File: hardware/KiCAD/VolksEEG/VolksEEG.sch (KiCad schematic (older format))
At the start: 0 parts

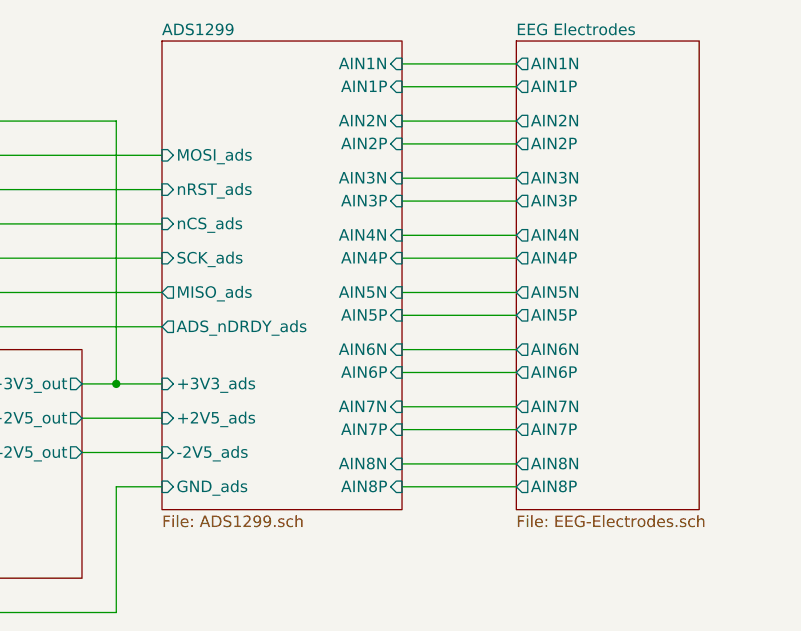
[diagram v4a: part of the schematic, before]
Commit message: Updating analogue inputs to the referential montage and connected a few ADS1299 pins.
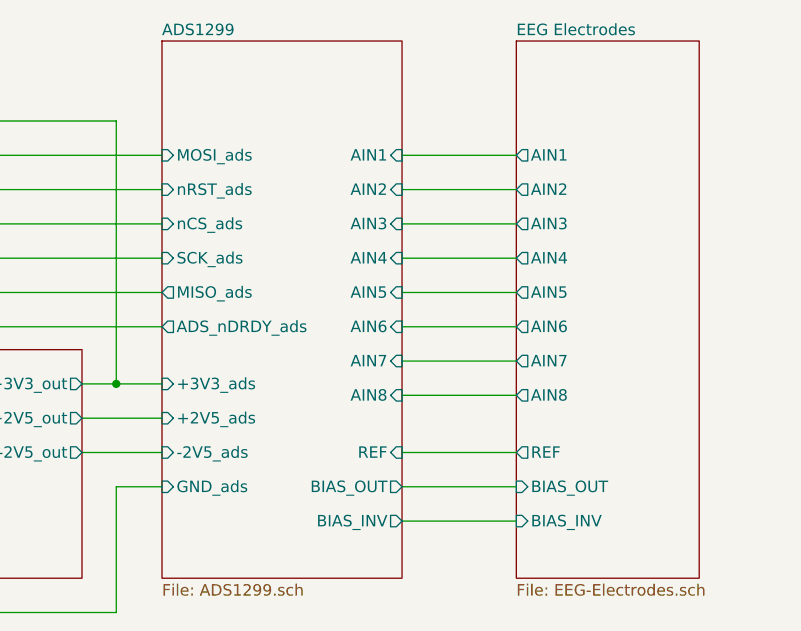
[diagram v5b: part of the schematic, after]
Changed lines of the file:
@@
 $EndDescr
 $Sheet
-S 6600 3000 1050 2050
+S 6600 3000 1050 2350
 U 615BA110
 F0 "ADS1299" 50
@@
 F5 "MISO_ads" O L 6600 4100 50
 F6 "nRST_ads" I L 6600 3650 50
-F7 "AIN5N" I R 7650 4100 50
-F8 "AIN5P" I R 7650 4200 50
-F9 "AIN6N" I R 7650 4350 50
-F10 "AIN6P" I R 7650 4450 50
-F11 "AIN7N" I R 7650 4600 50
-F12 "AIN7P" I R 7650 4700 50
-F13 "AIN8N" I R 7650 4850 50
-F14 "AIN8P" I R 7650 4950 50
-F15 "AIN1N" I R 7650 3100 50
-F16 "AIN1P" I R 7650 3200 50
-F17 "AIN2N" I R 7650 3350 50
-F18 "AIN2P" I R 7650 3450 50
-F19 "AIN3N" I R 7650 3600 50
-F20 "AIN3P" I R 7650 3700 50
-F21 "AIN4N" I R 7650 3850 50
-F22 "AIN4P" I R 7650 3950 50
-F23 "ADS_nDRDY_ads" O L 6600 4250 50
-F24 "+3V3_ads" I L 6600 4500 50
-F25 "+2V5_ads" I L 6600 4650 50
-F26 "-2V5_ads" I L 6600 4800 50
-F27 "GND_ads" I L 6600 4950 50
+F7 "AIN5" I R 7650 4100 50
+F8 "AIN6" I R 7650 4250 50
+F9 "AIN7" I R 7650 4400 50
+F10 "AIN8" I R 7650 4550 50
+F11 "AIN1" I R 7650 3500 50
+F12 "AIN2" I R 7650 3650 50
+F13 "AIN3" I R 7650 3800 50
+F14 "AIN4" I R 7650 3950 50
+F15 "ADS_nDRDY_ads" O L 6600 4250 50
+F16 "+3V3_ads" I L 6600 4500 50
+F17 "+2V5_ads" I L 6600 4650 50
+F18 "-2V5_ads" I L 6600 4800 50
+F19 "GND_ads" I L 6600 4950 50
+F20 "REF" I R 7650 4800 50
+F21 "BIAS_OUT" O R 7650 4950 50
+F22 "BIAS_INV" O R 7650 5100 50
 $EndSheet
 $Sheet
@@
 Wire Wire Line
 	2700 4100 3450 4100
-$Sheet
-S 8150 3000 800  2050
-U 615BA18D
-F0 "EEG Electrodes" 50
-F1 "EEG-Electrodes.sch" 50
-F2 "AIN2N" O L 8150 3350 50
-F3 "AIN1N" O L 8150 3100 50
-F4 "AIN1P" O L 8150 3200 50
-F5 "AIN2P" O L 8150 3450 50
-F6 "AIN3N" O L 8150 3600 50
-F7 "AIN3P" O L 8150 3700 50
-F8 "AIN4N" O L 8150 3850 50
-F9 "AIN4P" O L 8150 3950 50
-F10 "AIN5N" O L 8150 4100 50
-F11 "AIN5P" O L 8150 4200 50
-F12 "AIN6N" O L 8150 4350 50
-F13 "AIN6P" O L 8150 4450 50
-F14 "AIN7N" O L 8150 4600 50
-F15 "AIN7P" O L 8150 4700 50
-F16 "AIN8N" O L 8150 4850 50
-F17 "AIN8P" O L 8150 4950 50
-$EndSheet
-Wire Wire Line
-	7650 3100 8150 3100
-Wire Wire Line
-	8150 3200 7650 3200
-Wire Wire Line
-	8150 3350 7650 3350
-Wire Wire Line
-	7650 3450 8150 3450
-Wire Wire Line
-	8150 3600 7650 3600
-Wire Wire Line
-	7650 3700 8150 3700
-Wire Wire Line
-	8150 3850 7650 3850
-Wire Wire Line
-	7650 3950 8150 3950
 Wire Wire Line
 	8150 4100 7650 4100
-Wire Wire Line
-	7650 4200 8150 4200
-Wire Wire Line
-	8150 4350 7650 4350
-Wire Wire Line
-	7650 4450 8150 4450
-Wire Wire Line
-	8150 4600 7650 4600
-Wire Wire Line
-	7650 4700 8150 4700
-Wire Wire Line
-	8150 4850 7650 4850
-Wire Wire Line
-	7650 4950 8150 4950
 Wire Wire Line
 	4800 3500 6600 3500
@@
 	4950 5500 4950 4650
 Connection ~ 4950 4650
+$Sheet
+S 8150 3000 800  2350
+U 615BA18D
+F0 "EEG Electrodes" 50
+F1 "EEG-Electrodes.sch" 50
+F2 "AIN2" O L 8150 3650 50
+F3 "AIN1" O L 8150 3500 50
+F4 "AIN3" O L 8150 3800 50
+F5 "AIN4" O L 8150 3950 50
+F6 "AIN5" O L 8150 4100 50
+F7 "AIN6" O L 8150 4250 50
+F8 "AIN7" O L 8150 4400 50
+F9 "AIN8" O L 8150 4550 50
+F10 "REF" O L 8150 4800 50
+F11 "BIAS_OUT" I L 8150 4950 50
+F12 "BIAS_INV" I L 8150 5100 50
+$EndSheet
+Wire Wire Line
+	7650 3500 8150 3500
+Wire Wire Line
+	8150 3650 7650 3650
+Wire Wire Line
+	7650 3800 8150 3800
+Wire Wire Line
+	8150 3950 7650 3950
+Wire Wire Line
+	7650 4250 8150 4250
+Wire Wire Line
+	8150 4400 7650 4400
+Wire Wire Line
+	7650 4550 8150 4550
+Wire Wire Line
+	7650 4800 8150 4800
+Wire Wire Line
+	8150 4950 7650 4950
+Wire Wire Line
+	7650 5100 8150 5100
 $EndSCHEMATC
